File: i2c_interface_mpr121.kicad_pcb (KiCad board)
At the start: 2 copper layers, 15 x 11 mm, 0 parts

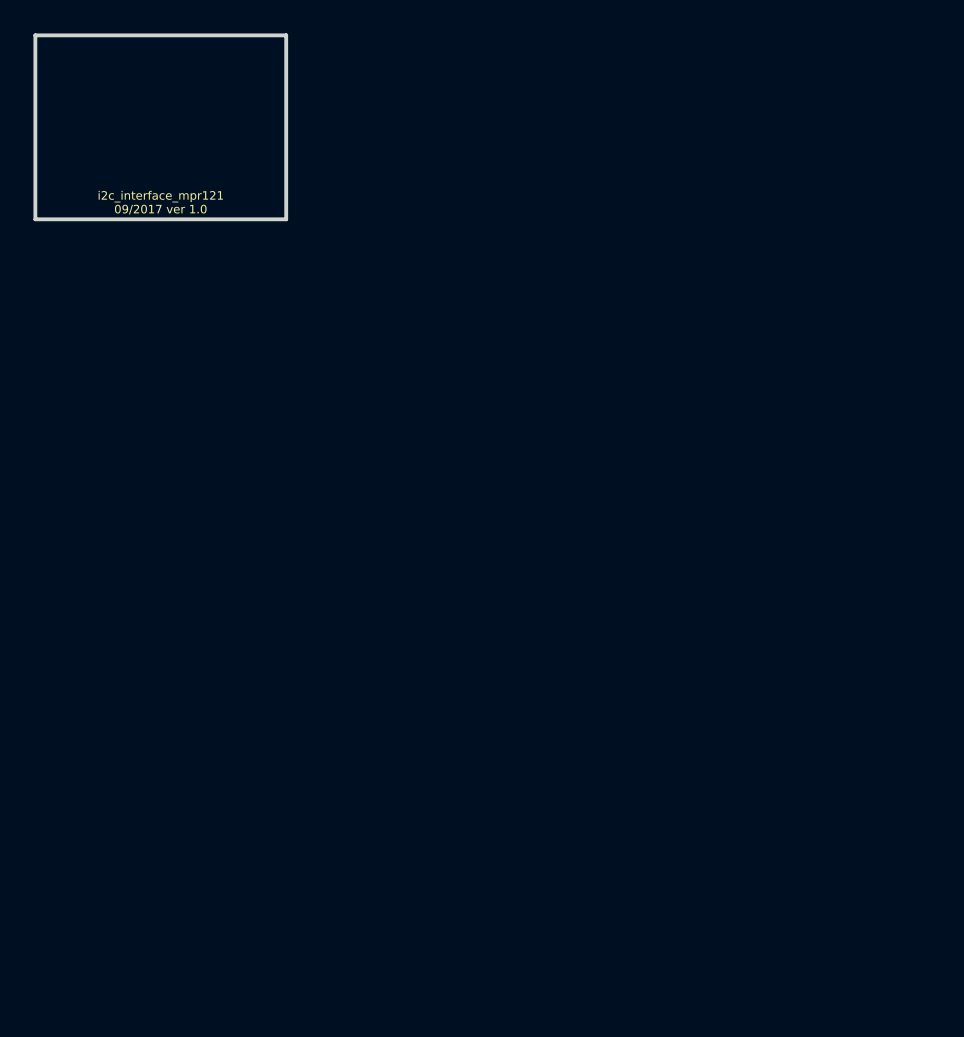
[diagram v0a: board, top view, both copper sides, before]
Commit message: Added footprints.
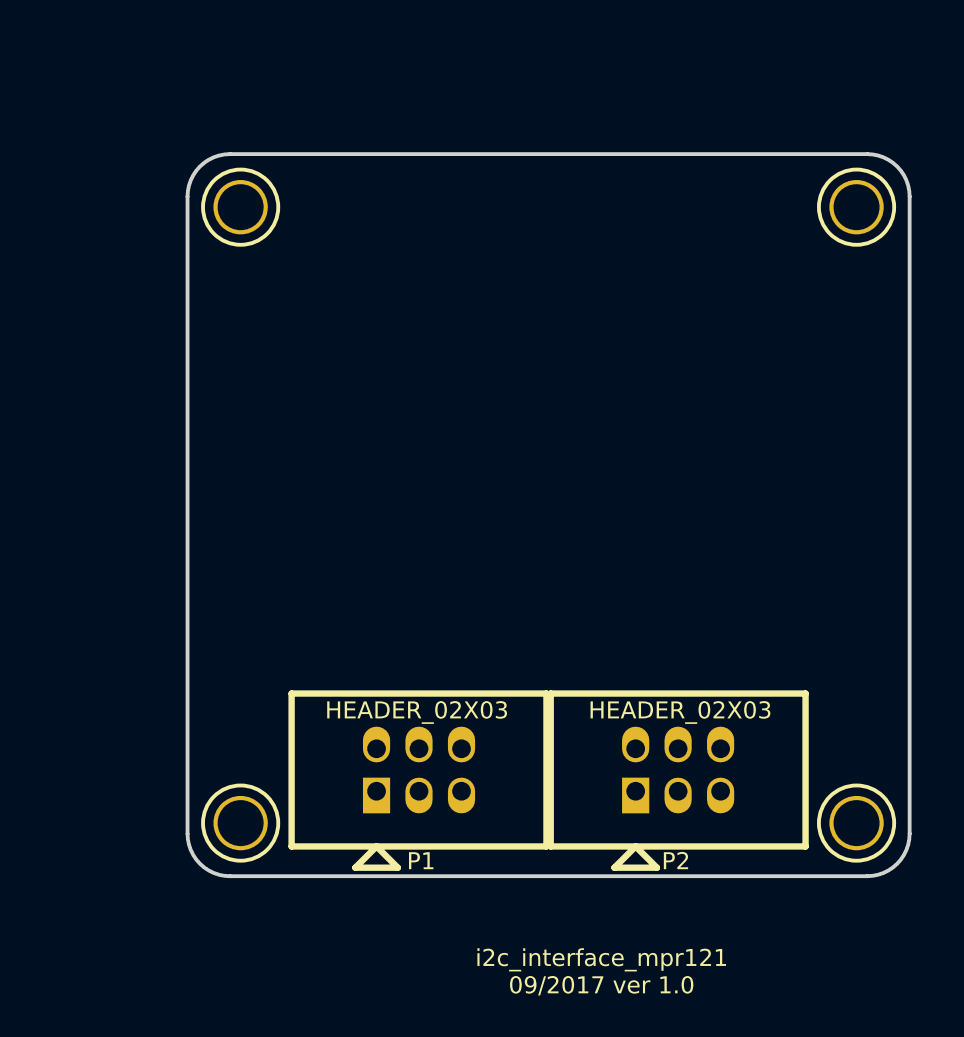
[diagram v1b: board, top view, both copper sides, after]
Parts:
- added P1: HEADER_02X03, i2c_interface_mpr121:HEADER_02x03, F.Cu at (115.4, 138.4)
- added P2: HEADER_02X03, i2c_interface_mpr121:HEADER_02x03, F.Cu at (130.9, 138.4)
- added SO1: STANDOFF_M2.5x0.45x8, i2c_interface_mpr121:MOUNTING_HOLE_M2.5, F.Cu at (104.8, 104.8)
- added SO2: STANDOFF_M2.5x0.45x8, i2c_interface_mpr121:MOUNTING_HOLE_M2.5, F.Cu at (104.8, 141.6)
- added SO3: STANDOFF_M2.5x0.45x8, i2c_interface_mpr121:MOUNTING_HOLE_M2.5, F.Cu at (141.6, 141.6)
- added SO4: STANDOFF_M2.5x0.45x8, i2c_interface_mpr121:MOUNTING_HOLE_M2.5, F.Cu at (141.6, 104.8)
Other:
- board size 15 x 11 mm -> 43.2 x 43.2 mm
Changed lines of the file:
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@@
   (general
     (thickness 1.6)
-    (drawings 5)
+    (drawings 9)
     (tracks 0)
     (zones 0)
-    (modules 0)
-    (nets 1)
+    (modules 6)
+    (nets 17)
   )
   (page A4)
@@
   )
   (net 0 "")
+  (net 1 "Net-(P1-Pad1)")
+  (net 2 "Net-(P1-Pad2)")
+  (net 3 "Net-(P1-Pad3)")
+  (net 4 "Net-(P1-Pad4)")
+  (net 5 "Net-(P1-Pad5)")
+  (net 6 "Net-(P1-Pad6)")
+  (net 7 "Net-(P2-Pad6)")
+  (net 8 "Net-(P2-Pad5)")
+  (net 9 "Net-(P2-Pad4)")
+  (net 10 "Net-(P2-Pad3)")
+  (net 11 "Net-(P2-Pad2)")
+  (net 12 "Net-(P2-Pad1)")
+  (net 13 "Net-(SO1-Pad1)")
+  (net 14 "Net-(SO2-Pad1)")
+  (net 15 "Net-(SO3-Pad1)")
+  (net 16 "Net-(SO4-Pad1)")
   (net_class Default "This is the default net class."
     (clearance 0.0254)
@@
     (uvia_dia 0.508)
     (uvia_drill 0.127)
+    (add_net "Net-(P1-Pad1)")
+    (add_net "Net-(P1-Pad2)")
+    (add_net "Net-(P1-Pad3)")
+    (add_net "Net-(P1-Pad4)")
+    (add_net "Net-(P1-Pad5)")
+    (add_net "Net-(P1-Pad6)")
+    (add_net "Net-(P2-Pad1)")
+    (add_net "Net-(P2-Pad2)")
+    (add_net "Net-(P2-Pad3)")
+    (add_net "Net-(P2-Pad4)")
+    (add_net "Net-(P2-Pad5)")
+    (add_net "Net-(P2-Pad6)")
+    (add_net "Net-(SO1-Pad1)")
+    (add_net "Net-(SO2-Pad1)")
+    (add_net "Net-(SO3-Pad1)")
+    (add_net "Net-(SO4-Pad1)")
   )
   (net_class GND ""
@@
     (diff_pair_width 0.254)
   )
-  (gr_line (start 107.5 94.5) (end 92.5 94.5) (angle 90) (layer Edge.Cuts) (width 0.2286))
-  (gr_line (start 107.5 105.5) (end 107.5 94.5) (angle 90) (layer Edge.Cuts) (width 0.2286))
-  (gr_line (start 92.5 105.5) (end 107.5 105.5) (angle 90) (layer Edge.Cuts) (width 0.2286))
-  (gr_line (start 92.5 94.5) (end 92.5 105.5) (angle 90) (layer Edge.Cuts) (width 0.2286))
-  (gr_text "i2c_interface_mpr121\n09/2017 ver 1.0" (at 100 104.5) (layer F.SilkS)
-    (effects (font (size 0.508 0.508) (thickness 0.127)))
+  (module i2c_interface_mpr121:HEADER_02x03 (layer F.Cu)
+    (at 115.443 138.43 180)
+    (fp_text reference P1 (at -0.127 -5.461 180) (layer F.SilkS)
+      (effects (font (size 1.016 1.016) (thickness 0.254)))
+    )
+    (fp_text value HEADER_02X03 (at 0.127 3.556) (layer F.SilkS)
+      (effects (font (size 1.016 1.016) (thickness 0.254)))
+    )
+    (fp_line (start -7.62 4.572) (end 7.62 4.572) (layer F.SilkS) (width 0.381))
+    (fp_line (start 7.62 -4.572) (end -7.62 -4.572) (layer F.SilkS) (width 0.381))
+    (fp_line (start -7.62 -4.572) (end -7.62 4.572) (layer F.SilkS) (width 0.381))
+    (fp_line (start 7.62 -4.572) (end 7.62 4.572) (layer F.SilkS) (width 0.381))
+    (fp_line (start 2.54 -4.572) (end 3.81 -5.842) (layer F.SilkS) (width 0.381))
+    (fp_line (start 3.81 -5.842) (end 1.27 -5.842) (layer F.SilkS) (width 0.381))
+    (fp_line (start 1.27 -5.842) (end 2.54 -4.572) (layer F.SilkS) (width 0.381))
+    (pad 1 thru_hole rect (at 2.54 -1.27 180) (size 1.6256 2.1336) (drill 1.1176 (offset 0 -0.254)) (layers *.Cu *.Mask F.SilkS)
+      (net 1 "Net-(P1-Pad1)"))
+    (pad 2 thru_hole oval (at 2.54 1.27 180) (size 1.6256 2.1336) (drill 1.1176 (offset 0 0.254)) (layers *.Cu *.Mask F.SilkS)
+      (net 2 "Net-(P1-Pad2)"))
+    (pad 3 thru_hole oval (at 0 -1.27 180) (size 1.6256 2.1336) (drill 1.1176 (offset 0 -0.254)) (layers *.Cu *.Mask F.SilkS)
+      (net 3 "Net-(P1-Pad3)"))
+    (pad 4 thru_hole oval (at 0 1.27 180) (size 1.6256 2.1336) (drill 1.1176 (offset 0 0.254)) (layers *.Cu *.Mask F.SilkS)
+      (net 4 "Net-(P1-Pad4)"))
+    (pad 5 thru_hole oval (at -2.54 -1.27 180) (size 1.6256 2.1336) (drill 1.1176 (offset 0 -0.254)) (layers *.Cu *.Mask F.SilkS)
+      (net 5 "Net-(P1-Pad5)"))
+    (pad 6 thru_hole oval (at -2.54 1.27 180) (size 1.6256 2.1336) (drill 1.1176 (offset 0 0.254)) (layers *.Cu *.Mask F.SilkS)
+      (net 6 "Net-(P1-Pad6)"))
+  )
+  (module i2c_interface_mpr121:HEADER_02x03 (layer F.Cu)
+    (at 130.937 138.43 180)
+    (fp_text reference P2 (at 0.127 -5.461 180) (layer F.SilkS)
+      (effects (font (size 1.016 1.016) (thickness 0.254)))
+    )
+    (fp_text value HEADER_02X03 (at -0.127 3.556) (layer F.SilkS)
+      (effects (font (size 1.016 1.016) (thickness 0.254)))
+    )
+    (fp_line (start 1.27 -5.842) (end 2.54 -4.572) (layer F.SilkS) (width 0.381))
+    (fp_line (start 3.81 -5.842) (end 1.27 -5.842) (layer F.SilkS) (width 0.381))
+    (fp_line (start 2.54 -4.572) (end 3.81 -5.842) (layer F.SilkS) (width 0.381))
+    (fp_line (start 7.62 -4.572) (end 7.62 4.572) (layer F.SilkS) (width 0.381))
+    (fp_line (start -7.62 -4.572) (end -7.62 4.572) (layer F.SilkS) (width 0.381))
+    (fp_line (start 7.62 -4.572) (end -7.62 -4.572) (layer F.SilkS) (width 0.381))
+    (fp_line (start -7.62 4.572) (end 7.62 4.572) (layer F.SilkS) (width 0.381))
+    (pad 6 thru_hole oval (at -2.54 1.27 180) (size 1.6256 2.1336) (drill 1.1176 (offset 0 0.254)) (layers *.Cu *.Mask F.SilkS)
+      (net 7 "Net-(P2-Pad6)"))
+    (pad 5 thru_hole oval (at -2.54 -1.27 180) (size 1.6256 2.1336) (drill 1.1176 (offset 0 -0.254)) (layers *.Cu *.Mask F.SilkS)
+      (net 8 "Net-(P2-Pad5)"))
+    (pad 4 thru_hole oval (at 0 1.27 180) (size 1.6256 2.1336) (drill 1.1176 (offset 0 0.254)) (layers *.Cu *.Mask F.SilkS)
+      (net 9 "Net-(P2-Pad4)"))
+    (pad 3 thru_hole oval (at 0 -1.27 180) (size 1.6256 2.1336) (drill 1.1176 (offset 0 -0.254)) (layers *.Cu *.Mask F.SilkS)
+      (net 10 "Net-(P2-Pad3)"))
+    (pad 2 thru_hole oval (at 2.54 1.27 180) (size 1.6256 2.1336) (drill 1.1176 (offset 0 0.254)) (layers *.Cu *.Mask F.SilkS)
+      (net 11 "Net-(P2-Pad2)"))
+    (pad 1 thru_hole rect (at 2.54 -1.27 180) (size 1.6256 2.1336) (drill 1.1176 (offset 0 -0.254)) (layers *.Cu *.Mask F.SilkS)
+      (net 12 "Net-(P2-Pad1)"))
+  )
+  (module i2c_interface_mpr121:MOUNTING_HOLE_M2.5 (layer F.Cu)
+    (at 104.775 104.775)
+    (fp_text reference SO1 (at 0 -3.175) (layer F.SilkS) hide
+      (effects (font (thickness 0.3048)))
+    )
+    (fp_text value STANDOFF_M2.5x0.45x8 (at 0 3.81) (layer F.SilkS) hide
+      (effects (font (thickness 0.3048)))
+    )
+    (fp_circle (center 0 0) (end 2.6 0) (layer B.SilkS) (width 0.2286))
+    (fp_circle (center 0 0) (end 2.25 0) (layer F.SilkS) (width 0.2286))
+    (pad 1 thru_hole circle (at 0 0) (size 3.25 3.25) (drill 2.75) (layers *.Cu *.Mask F.SilkS)
+      (net 13 "Net-(SO1-Pad1)"))
+  )
+  (module i2c_interface_mpr121:MOUNTING_HOLE_M2.5 (layer F.Cu)
+    (at 104.775 141.605)
+    (fp_text reference SO2 (at 0 -3.175) (layer F.SilkS) hide
+      (effects (font (thickness 0.3048)))
+    )
+    (fp_text value STANDOFF_M2.5x0.45x8 (at 0 3.81) (layer F.SilkS) hide
+      (effects (font (thickness 0.3048)))
+    )
+    (fp_circle (center 0 0) (end 2.25 0) (layer F.SilkS) (width 0.2286))
+    (fp_circle (center 0 0) (end 2.6 0) (layer B.SilkS) (width 0.2286))
+    (pad 1 thru_hole circle (at 0 0) (size 3.25 3.25) (drill 2.75) (layers *.Cu *.Mask F.SilkS)
+      (net 14 "Net-(SO2-Pad1)"))
+  )
+  (module i2c_interface_mpr121:MOUNTING_HOLE_M2.5 (layer F.Cu)
+    (at 141.605 141.605)
+    (fp_text reference SO3 (at 0 -3.175) (layer F.SilkS) hide
+      (effects (font (thickness 0.3048)))
+    )
+    (fp_text value STANDOFF_M2.5x0.45x8 (at 0 3.81) (layer F.SilkS) hide
+      (effects (font (thickness 0.3048)))
+    )
+    (fp_circle (center 0 0) (end 2.6 0) (layer B.SilkS) (width 0.2286))
+    (fp_circle (center 0 0) (end 2.25 0) (layer F.SilkS) (width 0.2286))
+    (pad 1 thru_hole circle (at 0 0) (size 3.25 3.25) (drill 2.75) (layers *.Cu *.Mask F.SilkS)
+      (net 15 "Net-(SO3-Pad1)"))
+  )
+  (module i2c_interface_mpr121:MOUNTING_HOLE_M2.5 (layer F.Cu)
+    (at 141.605 104.775)
+    (fp_text reference SO4 (at 0 -3.175) (layer F.SilkS) hide
+      (effects (font (thickness 0.3048)))
+    )
+    (fp_text value STANDOFF_M2.5x0.45x8 (at 0 3.81) (layer F.SilkS) hide
+      (effects (font (thickness 0.3048)))
+    )
+    (fp_circle (center 0 0) (end 2.25 0) (layer F.SilkS) (width 0.2286))
+    (fp_circle (center 0 0) (end 2.6 0) (layer B.SilkS) (width 0.2286))
+    (pad 1 thru_hole circle (at 0 0) (size 3.25 3.25) (drill 2.75) (layers *.Cu *.Mask F.SilkS)
+      (net 16 "Net-(SO4-Pad1)"))
+  )
+  (gr_line (start 142.24 101.6) (end 104.14 101.6) (angle 90) (layer Edge.Cuts) (width 0.2286))
+  (gr_line (start 144.78 142.24) (end 144.78 104.14) (angle 90) (layer Edge.Cuts) (width 0.2286))
+  (gr_line (start 104.14 144.78) (end 142.24 144.78) (angle 90) (layer Edge.Cuts) (width 0.2286))
+  (gr_line (start 101.6 104.14) (end 101.6 142.24) (angle 90) (layer Edge.Cuts) (width 0.2286))
+  (gr_arc (start 142.24 104.14) (end 142.24 101.6) (angle 90) (layer Edge.Cuts) (width 0.2286))
+  (gr_arc (start 142.24 142.24) (end 144.78 142.24) (angle 90) (layer Edge.Cuts) (width 0.2286))
+  (gr_arc (start 104.14 142.24) (end 104.14 144.78) (angle 90) (layer Edge.Cuts) (width 0.2286))
+  (gr_arc (start 104.14 104.14) (end 101.6 104.14) (angle 90) (layer Edge.Cuts) (width 0.2286))
+  (gr_text "i2c_interface_mpr121\n09/2017 ver 1.0" (at 126.365 150.495) (layer F.SilkS)
+    (effects (font (size 1.016 1.016) (thickness 0.254)))
   )
 )

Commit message: Progress towards v1.0.
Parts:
- added AF1: ADAFRUIT_MPR121, i2c_interface_mpr121:ADAFRUIT_MPR121, F.Cu at (123.2, 120.7)
- added C1: 0.1uF, i2c_interface_mpr121:SM1210, B.Cu at (125.1, 138.4)
- added T1: TERM_BLK_12_PIN_0.1_PITCH, i2c_interface_mpr121:TERM_BLK_12_PIN_0.1_PITCH, F.Cu at (123.2, 104.8)
- added U1: PCA9615, i2c_interface_mpr121:TSSOP10, B.Cu at (120.7, 138.4)
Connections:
- P1 pad 1: Net-(P1-Pad1) -> /DSCLP
- P1 pad 2: Net-(P1-Pad2) -> /DSCLM
- P1 pad 3: Net-(P1-Pad3) -> VEE
- P1 pad 4: Net-(P1-Pad4) -> GND
- P1 pad 5: Net-(P1-Pad5) -> /DSDAP
- P1 pad 6: Net-(P1-Pad6) -> /DSDAM
- P2 pad 1: Net-(P2-Pad1) -> /DSCLP
- P2 pad 2: Net-(P2-Pad2) -> /DSCLM
- P2 pad 3: Net-(P2-Pad3) -> VEE
- P2 pad 4: Net-(P2-Pad4) -> GND
- P2 pad 5: Net-(P2-Pad5) -> /DSDAP
- P2 pad 6: Net-(P2-Pad6) -> /DSDAM
- SO1 pad 1: Net-(SO1-Pad1) -> (no net)
- SO2 pad 1: Net-(SO2-Pad1) -> (no net)
- SO3 pad 1: Net-(SO3-Pad1) -> (no net)
- SO4 pad 1: Net-(SO4-Pad1) -> (no net)
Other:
- board text added: "0"
- board text added: "1"
- board text added: "10"
- board text added: "11"
- board text added: "2"
- board text added: "3"
- board text added: "4"
- board text added: "5"
- board text added: "6"
- board text added: "7"
- board text added: "8"
- board text added: "9"

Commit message: Finished v1.0.
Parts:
- added S1: HEADER_01X02, i2c_interface_mpr121:HEADER_01x02, F.Cu at (104.8, 120.0)
- added S2: HEADER_01X02, i2c_interface_mpr121:HEADER_01x02, F.Cu at (104.8, 126.4)
- added S3: HEADER_01X02, i2c_interface_mpr121:HEADER_01x02, F.Cu at (104.8, 132.7)
- moved AF1 2.84 mm to (124.5, 118.1)
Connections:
- AF1 pad 17: Net-(AF1-Pad17) -> /ADDR
- AF1 pad 20: Net-(AF1-Pad20) -> (no net)
- SO1 pad 1: (no net) -> Net-(SO1-Pad1)
- SO2 pad 1: (no net) -> Net-(SO2-Pad1)
- SO3 pad 1: (no net) -> Net-(SO3-Pad1)
- SO4 pad 1: (no net) -> Net-(SO4-Pad1)
- U1 pad 3: Net-(U1-Pad3) -> (no net)
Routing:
- net VEE: track 0.00 -> 71.3 mm
- net GND: track 0.00 -> 49.1 mm
- net /ADDR: track 0.00 -> 37.9 mm
- net /SDA: track 0.00 -> 36.7 mm
- net /SCL: track 0.00 -> 29.9 mm
- net /DSCLP: track 0.00 -> 26.7 mm
- net /DSCLM: track 0.00 -> 25.6 mm
- net /DSDAM: track 0.00 -> 23.5 mm
- net /DSDAP: track 0.00 -> 22.9 mm
- net /IN_9: track 0.00 -> 5.08 mm
- net /IN_8: track 0.00 -> 5.08 mm
- net /IN_7: track 0.00 -> 5.08 mm
- net /IN_6: track 0.00 -> 5.08 mm
- net /IN_5: track 0.00 -> 5.08 mm
- net /IN_4: track 0.00 -> 5.08 mm
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- added copper zone on B.Cu, net GND
- added copper zone on F.Cu, net VEE
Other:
- net class Default: trace_width 0.25 -> 0.254
- net class GND: trace_width 0.4064 -> 0.3048
- net class POWER: clearance 0.254 -> 0.1016; trace_width 0.8128 -> 0.3048
- net class SIGNAL: trace_width 0.4064 -> 0.3048
- board text added: "0x5A"
- board text added: "0x5B"
- board text added: "0x5C"
- board text added: "0x5D"
- board text added: "Default"
- board text added: "I2C ADDRESS"
- board text removed: "0"
- board text removed: "1"
- board text removed: "10"
- board text removed: "11"
- board text removed: "2"
- board text removed: "3"
- board text removed: "4"
- board text removed: "5"
- board text removed: "6"
- board text removed: "7"
- board text removed: "8"
- board text removed: "9"
